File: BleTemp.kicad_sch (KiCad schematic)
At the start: 24 parts, among them SW1 TS-1088-AR02016, U1 NRF52832-QFAA-R, X1 32MHz, X2 32.768KHz

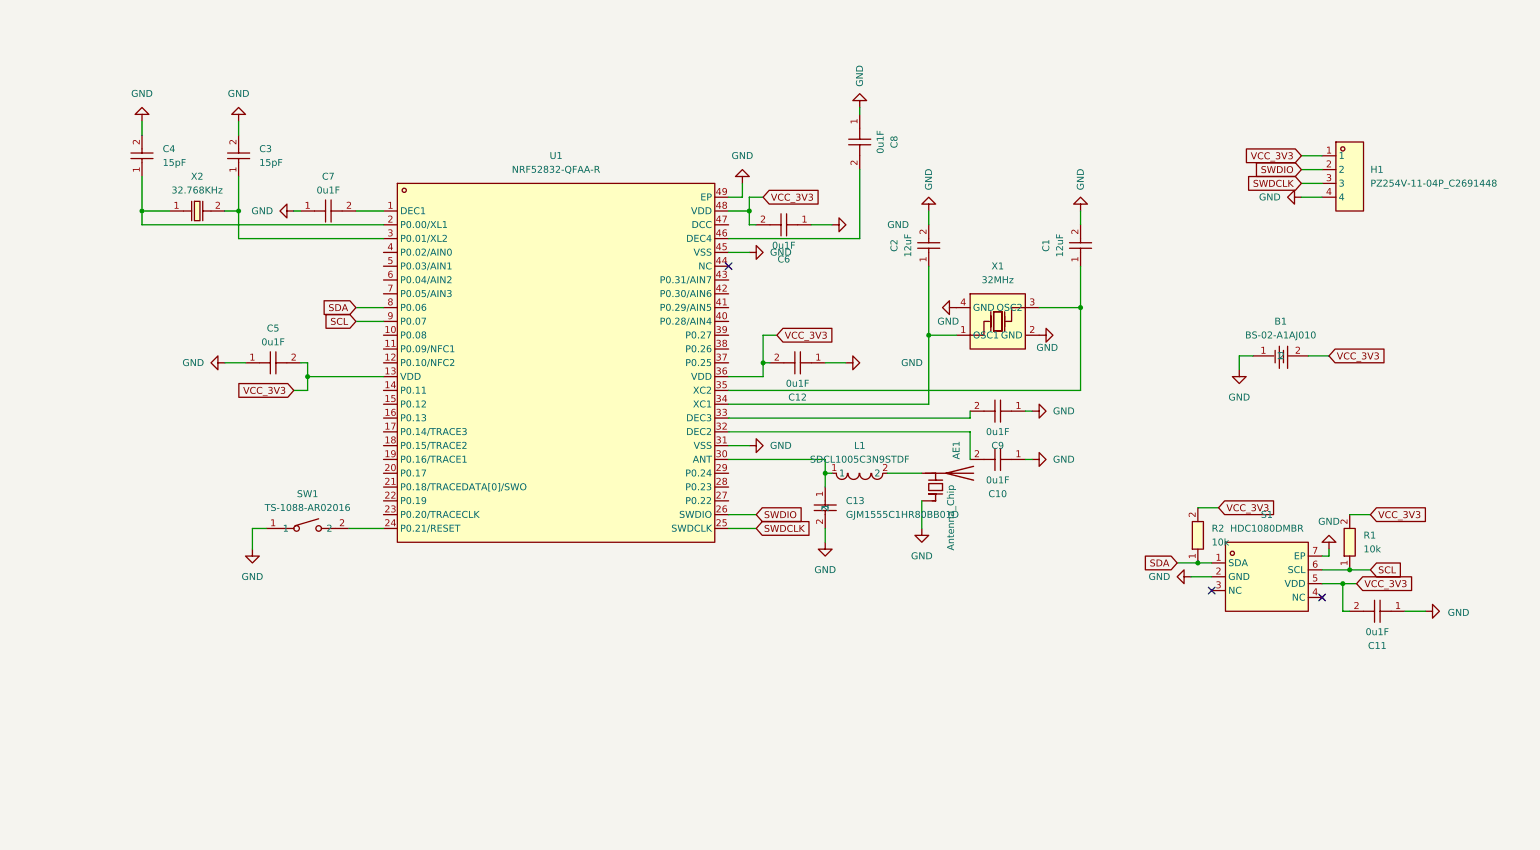
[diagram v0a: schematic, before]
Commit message: add copper zones
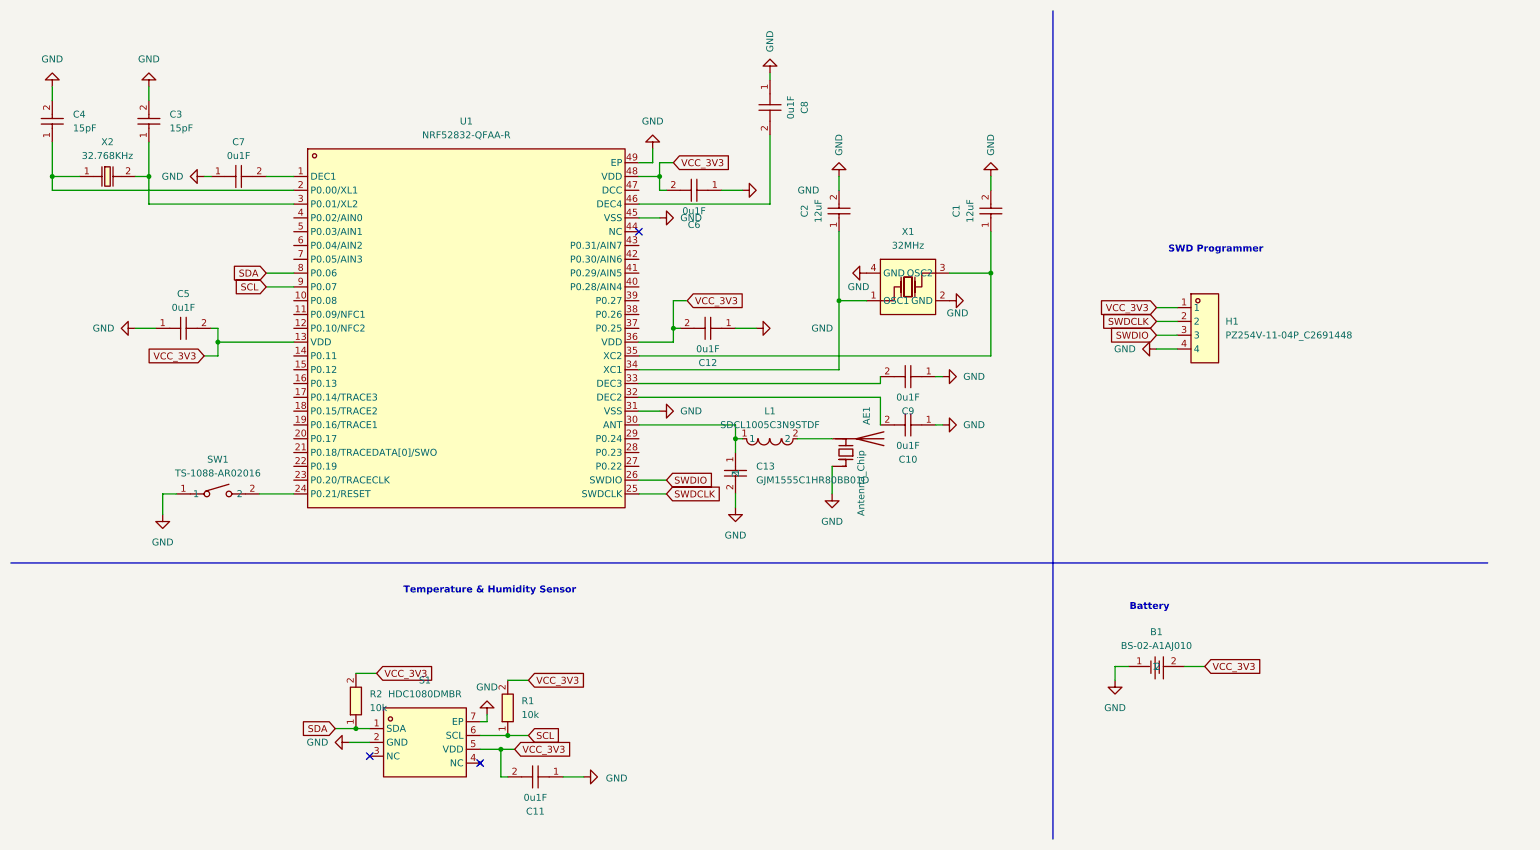
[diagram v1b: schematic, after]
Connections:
- net SWDCLK: now also H1.2; no longer H1.3
- net SWDIO: now also H1.3; no longer H1.2
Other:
- note added: "Battery"
- note added: "SWD Programmer"
- note added: "Temperature & Humidity Sensor"
- moved on the sheet: AE1, B1, C1, C10, C11, C12, C13, C2, C3, C4, C5, C6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
